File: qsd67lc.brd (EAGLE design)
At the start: 160 x 100 mm, 65 parts, among them CON1 RIA-AKL-230-04, CON2 RIA-AKL-230-04, CON3 RIA-AKL-230-03, IC1 MEGA8-P, IC2 BTS555E3146, IC3 MAX3232CPE, IC4 LM2576S, IC5 FT232RL, IC6 ISO7221A, T1 BCR141, U1 HC_05, X2 RS232

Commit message: first placement of all parts
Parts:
- LED4: value (none) -> green
- LED5: value (none) -> orange
- moved C17 401.5 mm to (67.3, 26.7)
- moved C18 401.5 mm to (67.3, 20.3), flipped to the bottom, turned to 180 degrees
- moved IC6 387.4 mm to (67.3, 20.3), turned to 180 degrees
- moved C15 366.9 mm to (57.1, 29.2)
- moved C16 359.5 mm to (66.0, 8.89)
- moved R19 353.1 mm to (68.6, 12.7)
- moved R18 344.8 mm to (61.0, 12.7)
- moved LED5 341.1 mm to (69.8, 8.89), turned to 270 degrees
- moved C14 333.0 mm to (57.1, 17.8), turned to 180 degrees
- moved LED4 332.8 mm to (62.2, 8.89), turned to 270 degrees
- moved C13 331.9 mm to (57.1, 21.6)
- moved R10 281.7 mm to (29.2, 41.9), flipped to the bottom, turned to 90 degrees
- moved IC5 281.5 mm to (57.1, 20.3), turned to 90 degrees
- moved S1 134.6 mm to (64.8, 47.0), turned to 180 degrees
- moved R4 129.5 mm to (57.1, 2.54)
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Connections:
- net N$25 renamed USB_TX_LED
- net RS232_RX: no longer IC6.2
- net RS232_TX: no longer IC6.3
- net RXD_RS232: now also IC6.2
- net TXD_RS232: now also IC6.3
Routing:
- net 12V_OUT: track 18.3 -> 14.3 mm
- added copper zone on layer 1, net GND
- added copper zone on layer 16, net GND

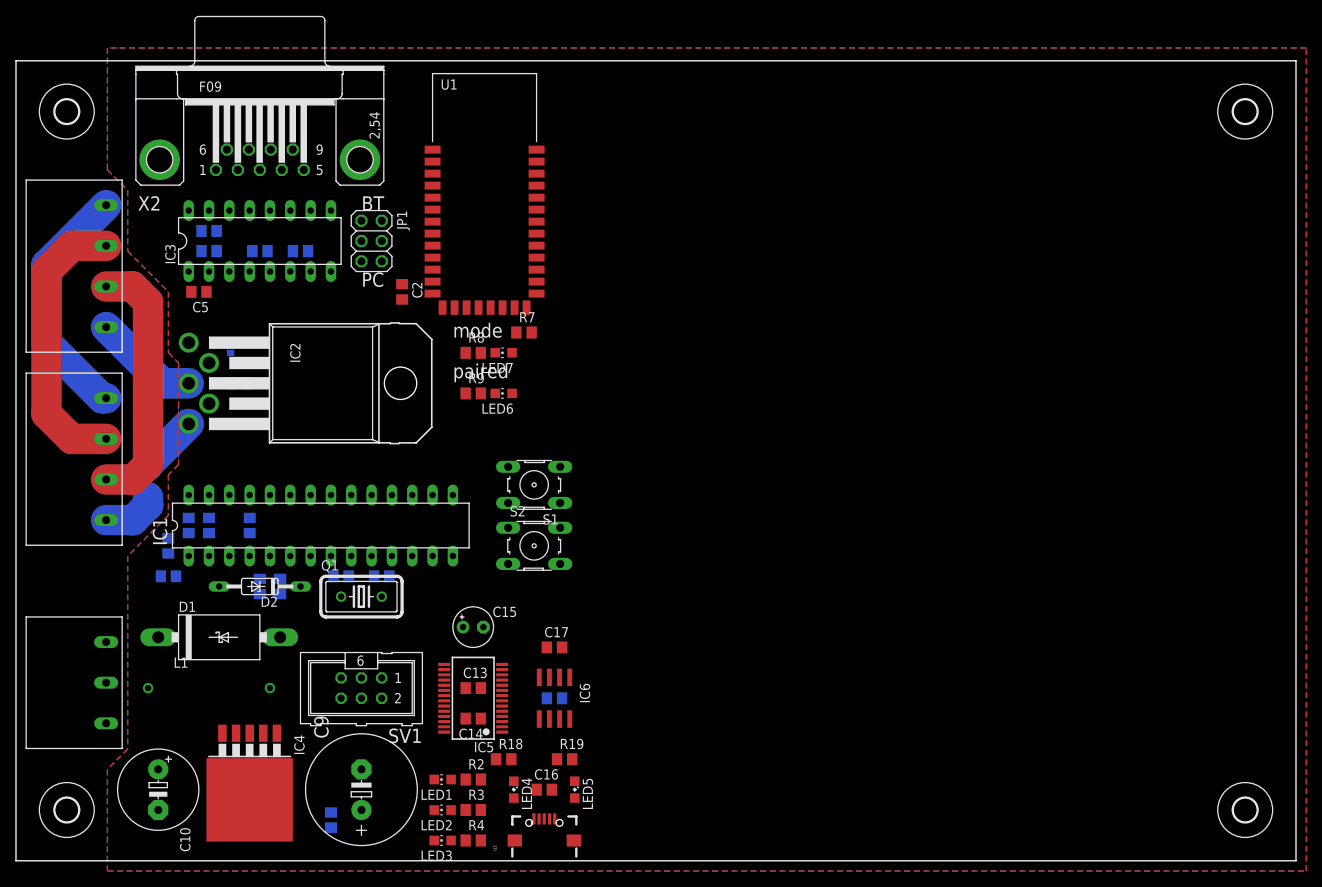
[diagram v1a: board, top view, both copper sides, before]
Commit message: working commit: * moved drill hole * removed 1 button * replaced status leds * moved ground planes
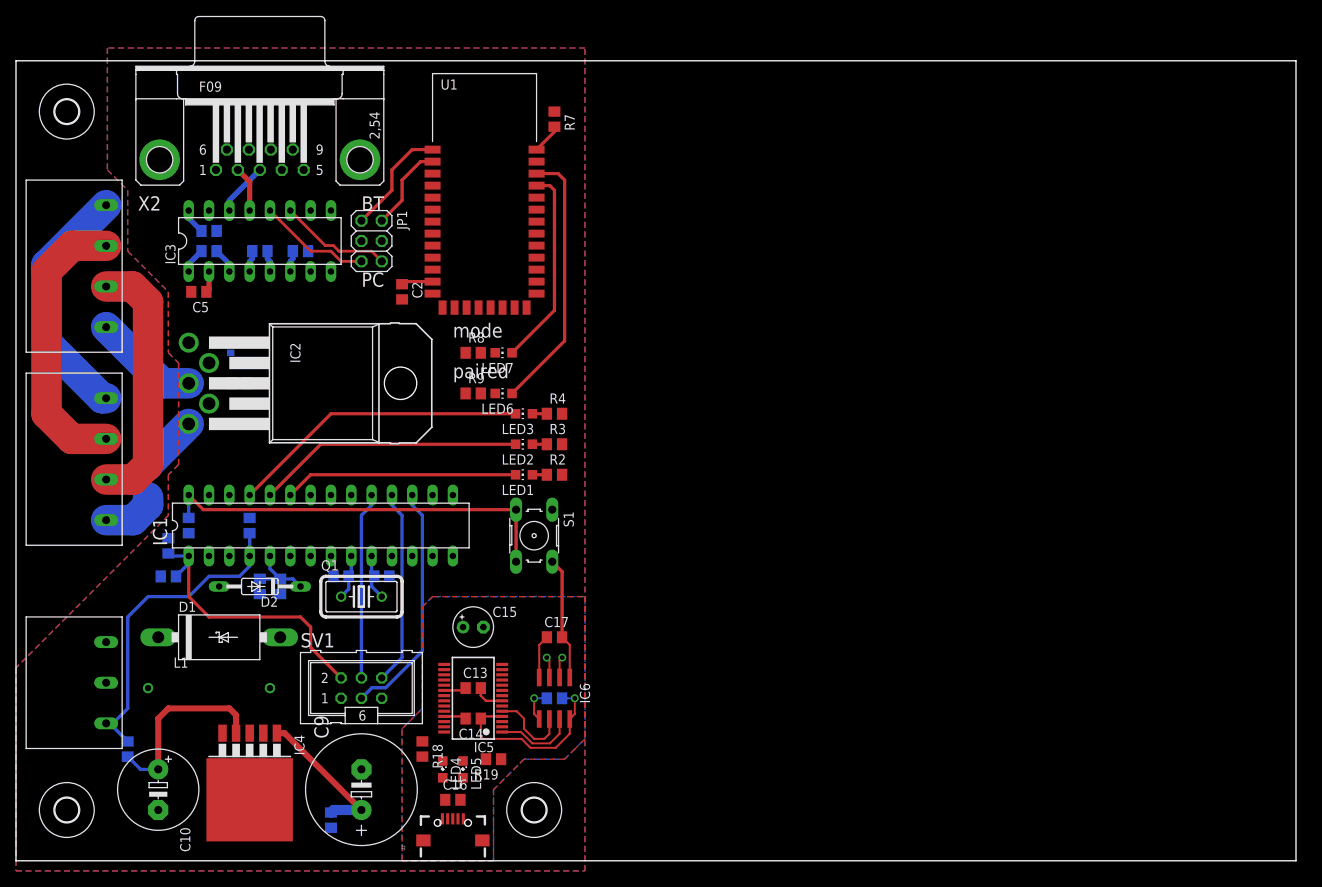
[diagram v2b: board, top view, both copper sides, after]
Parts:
- removed H2: MOUNT-HOLE3.0, holes:3,0
- removed R5: 10k, rcl:R0805
- removed S2: (no value), switch-omron:B3F-10XX
- added R14: 10k, rcl:R0805
- moved H3 88.9 mm to (64.8, 6.35)
- moved LED3 54.3 mm to (63.5, 55.9)
- moved R4 54.3 mm to (67.3, 55.9)
- moved LED2 46.8 mm to (63.5, 52.1)
- moved R3 46.8 mm to (67.3, 52.1)
- moved LED1 39.4 mm to (63.5, 48.3)
- moved R2 39.4 mm to (67.3, 48.3)
- moved R7 26.9 mm to (67.3, 92.7), turned to 270 degrees
- moved LED5 14.2 mm to (55.9, 11.4)
- moved C16 11.5 mm to (54.6, 7.62)
- moved U2 11.4 mm to (54.6, 2.54)
- moved R18 10.2 mm to (50.8, 14.0), turned to 270 degrees
- moved LED4 9.25 mm to (53.3, 11.4)
- moved R19 8.89 mm to (59.7, 12.7), turned to 180 degrees
- moved S1 6.35 mm to (64.8, 40.6), turned to 270 degrees
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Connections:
- removed net IGN0_IN: R13.2
- removed net N$8: IC1.27, R5.2, S2.3, S2.4
- net +3V3: now also R14.2; no longer S2.1, S2.2
- net GND: no longer R5.1
- net IGN0: now also R13.2
- net QS+: now also R14.1
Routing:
- net N$12: track 0.00 -> 51.0 mm
- net +3V3: track 0.00 -> 46.2 mm
- net QS+: track 0.00 -> 40.5 mm
- net N$9: track 0.00 -> 37.4 mm
- net RESET: track 0.00 -> 35.7 mm
- net N$1: track 0.00 -> 33.3 mm
- net PAIRED_STATE: track 0.00 -> 33.2 mm
- net MOSI: track 0.00 -> 30.1 mm
- net N$7: track 0.00 -> 29.2 mm
- net WORK_MODE: track 0.00 -> 25.0 mm
- net MISO: track 0.00 -> 24.4 mm
- net VCCIO_USB: track 0.00 -> 23.7 mm, vias 0 -> 1
- net SCK: track 0.00 -> 23.4 mm
- net +12V: track 13.2 -> 31.7 mm
- net RXD_RS232: track 0.00 -> 16.7 mm, vias 0 -> 1
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- added copper zone on layer 1, net GND_USB
- added copper zone on layer 16, net GND_USB

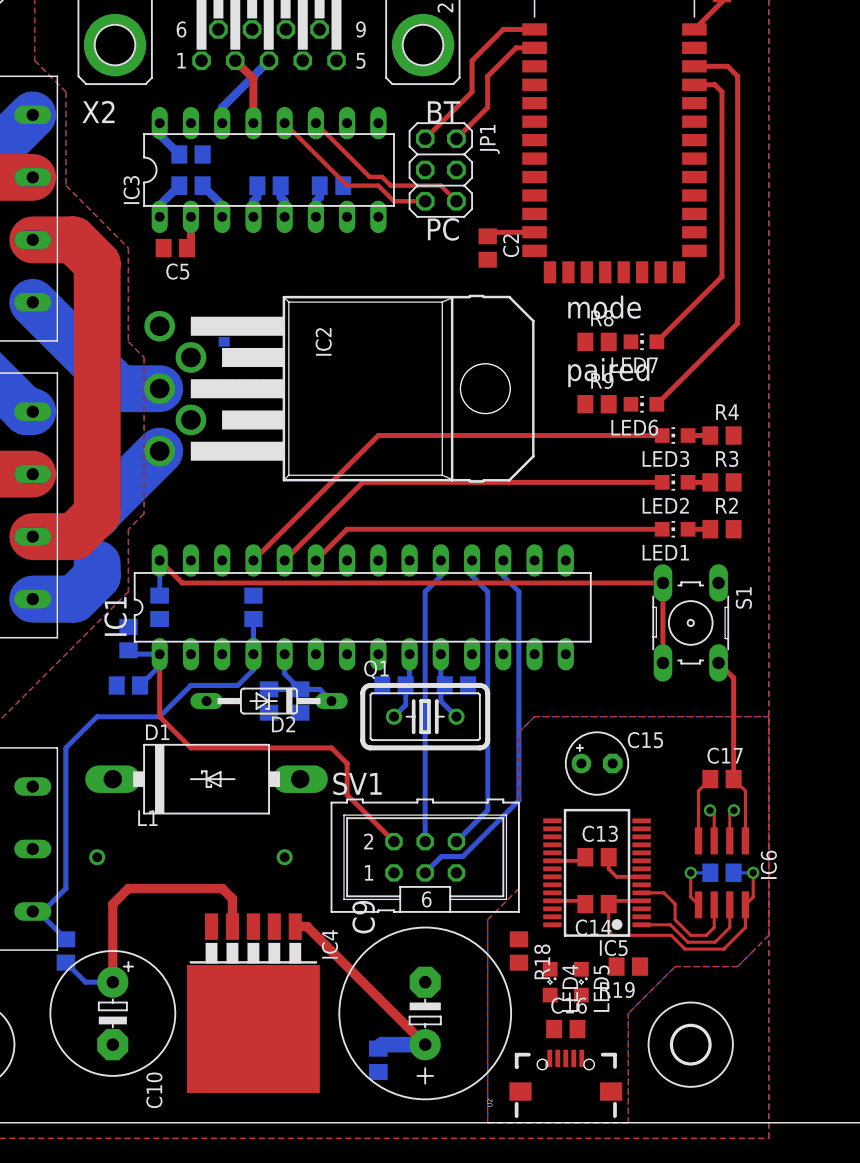
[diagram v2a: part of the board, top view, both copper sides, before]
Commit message: routed ftdi part
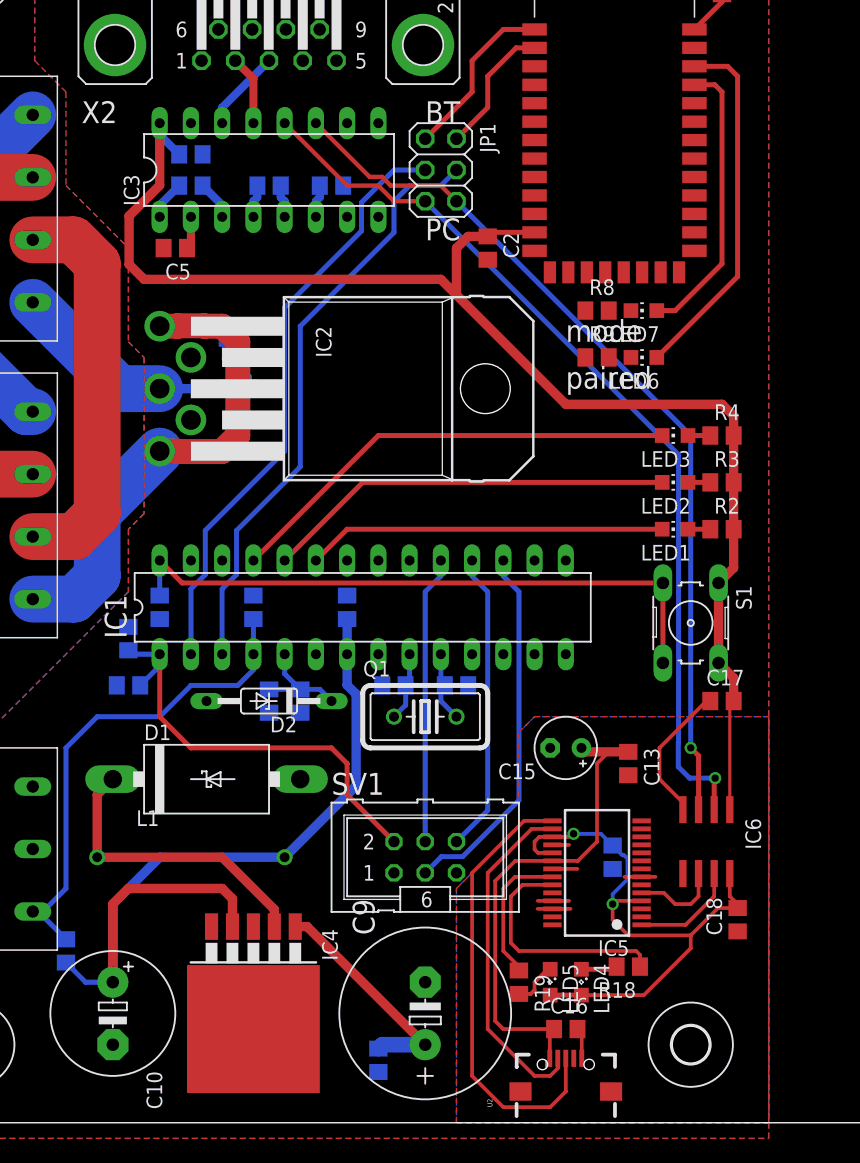
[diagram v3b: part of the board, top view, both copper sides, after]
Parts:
- added C19: 100n, rcl:C0805
- moved R18 8.98 mm to (59.7, 12.7), turned to 180 degrees
- moved R19 8.98 mm to (50.8, 11.4), turned to 270 degrees
- moved C13 8.03 mm to (59.7, 29.2), turned to 270 degrees
- moved C17 6.35 mm to (67.3, 34.3)
- moved C14 4.02 mm to (58.4, 21.6), flipped to the bottom, turned to 270 degrees
- moved C18 4.02 mm to (68.6, 16.5), flipped to the top, turned to 90 degrees
- moved LED6 3.81 mm to (61.0, 62.2)
- moved R9 3.81 mm to (57.1, 62.2)
- moved C15 2.84 mm to (54.6, 30.5), turned to 180 degrees
- moved IC6 2.84 mm to (66.0, 22.9)
- moved LED7 2.54 mm to (61.0, 66.0)
- moved R8 2.54 mm to (57.1, 66.0)
- moved LED4 2.54 mm to (55.9, 11.4)
- moved LED5 2.54 mm to (53.3, 11.4)
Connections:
- net +3V3: now also C19.1
- net GND: now also C19.2
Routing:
- net +3V3: track 46.2 -> 181.5 mm
- net RXD_RS232: track 16.7 -> 74.7 mm
- net TXD_RS232: track 16.7 -> 71.7 mm
- net TXD: track 0.00 -> 48.7 mm
- net RXD: track 0.00 -> 48.7 mm
- net VCC_USB: track 2.80 -> 41.8 mm
- net USB_D+: track 0.00 -> 36.7 mm
- net USB_D-: track 0.00 -> 27.8 mm
- net 12V_OUT: track 14.3 -> 39.7 mm
- net N$22: track 0.00 -> 24.4 mm
- net VCCIO_USB: track 23.7 -> 48.0 mm, vias 1 -> 2
- net USB_RX_LED: track 0.00 -> 19.4 mm
- net USB_TX_LED: track 0.00 -> 11.6 mm
- net GND: track 5.42 -> 11.5 mm
- net +12V: track 31.7 -> 37.1 mm
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
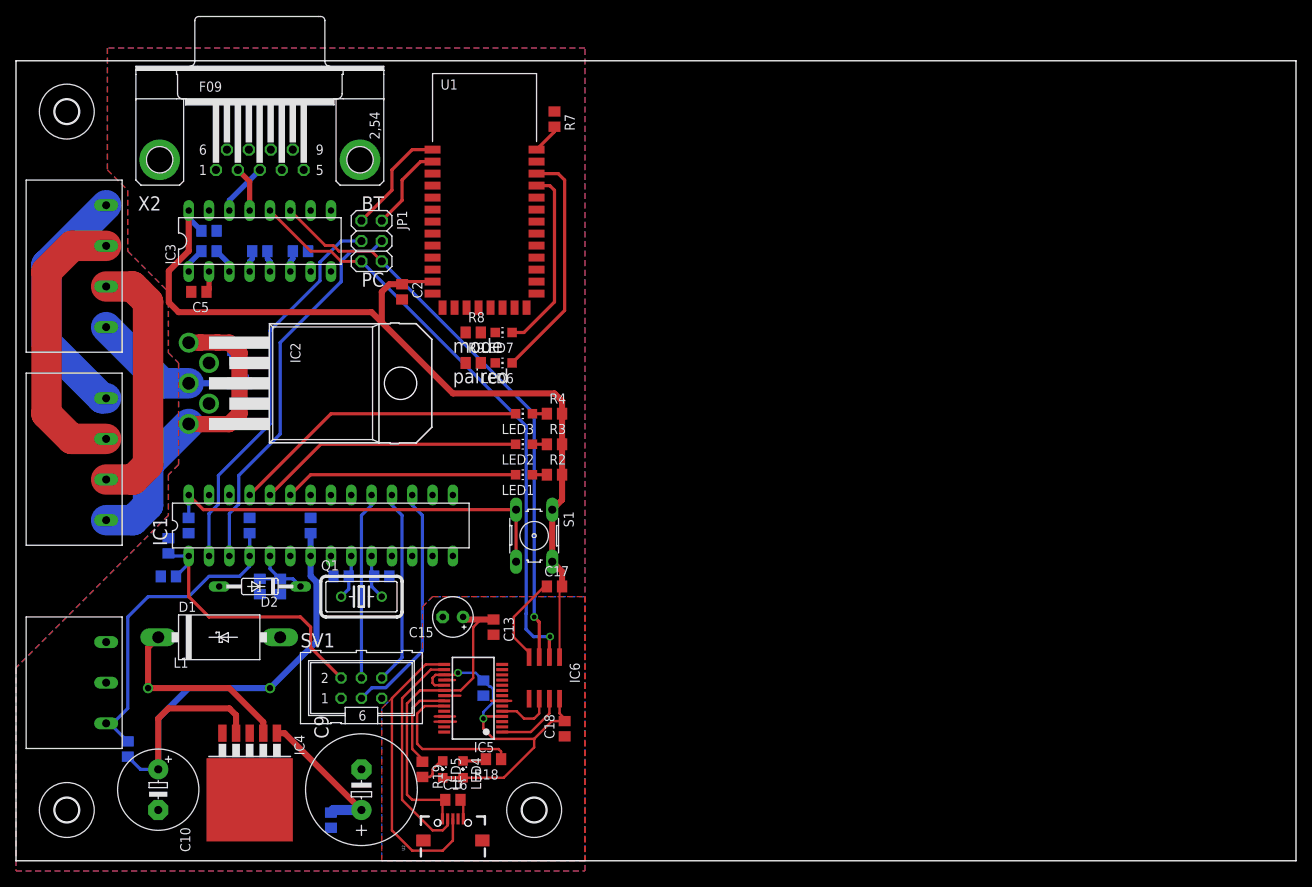
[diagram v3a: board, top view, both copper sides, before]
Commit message: finished layout added some test probe pins to 3v3 12V and GND added lables to leds, connectors and pinheads
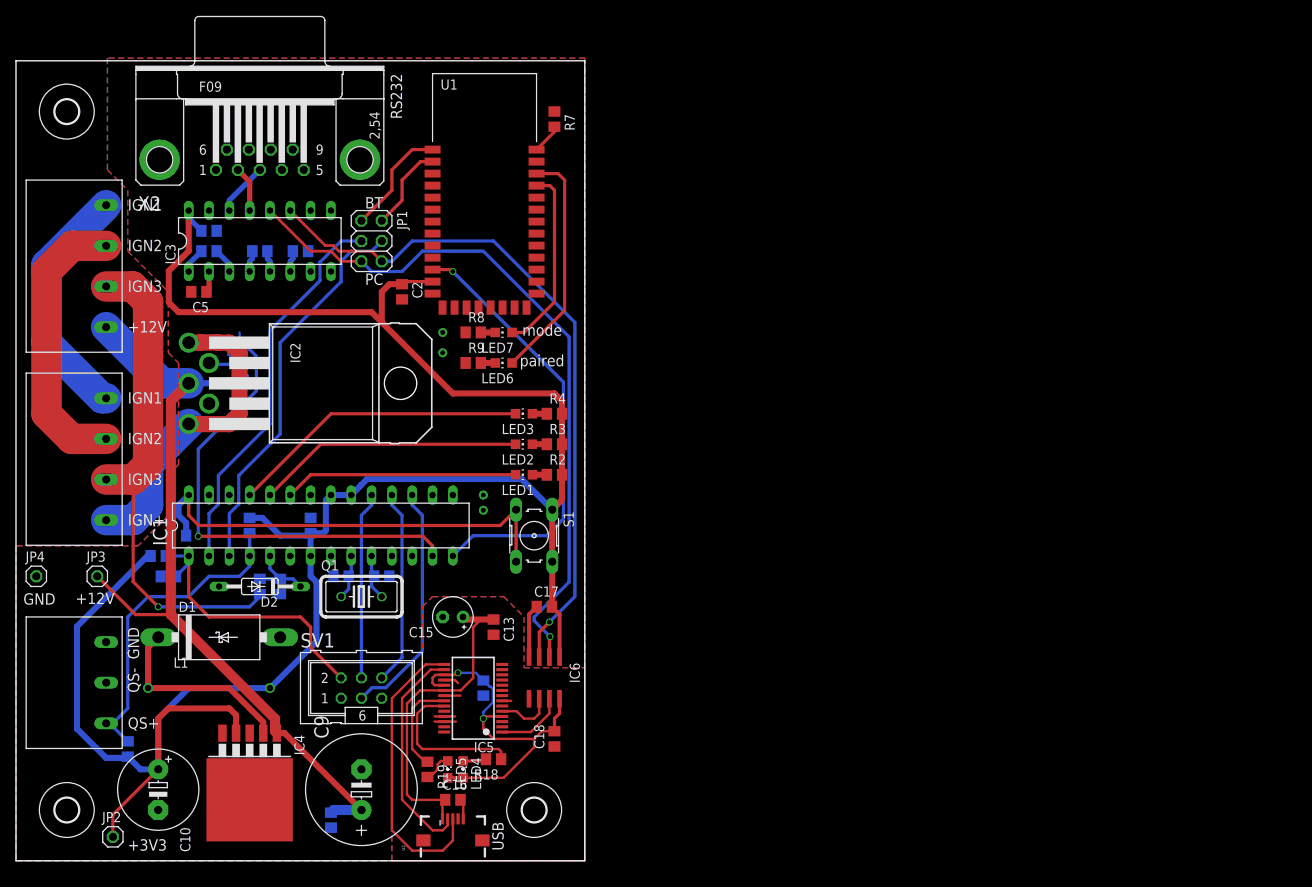
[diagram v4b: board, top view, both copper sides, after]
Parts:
- added JP2, JP3, JP4: (no value), pinhead:1X01
- moved C17 2.84 mm to (66.0, 31.8)
- moved C18 1.80 mm to (67.3, 15.2)
- moved R1 1.80 mm to (17.8, 38.1), turned to 0 degrees
- moved R6 1.80 mm to (20.3, 40.6), turned to 180 degrees
- moved R19 0.64 mm to (51.4, 11.4)
- moved LED5 0.63 mm to (54.0, 11.4)
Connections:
- net +12V: now also JP3.1
- net +3V3: now also JP2.1
- net GND: now also JP4.1
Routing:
- net +3V3: track 181.5 -> 271.2 mm
- net +12V: track 37.1 -> 98.4 mm
- net IGN_CTL: track 0.00 -> 58.4 mm, vias 0 -> 1
- net HC05_RST: track 0.00 -> 55.0 mm, vias 0 -> 1
- net IGN0: track 32.4 -> 63.1 mm, vias 0 -> 1
- net TXD_RS232: track 71.7 -> 87.1 mm
- net RXD_RS232: track 74.7 -> 88.7 mm
- net N$12: track 51.0 -> 57.3 mm
- net N$16: track 5.03 -> 7.81 mm
- net N$14: track 0.00 -> 1.81 mm
- net N$13: track 0.00 -> 1.81 mm
- net VCCIO_USB: track 48.0 -> 46.4 mm
- net GND_USB: track 13.6 -> 12.8 mm
- net GND: track 11.5 -> 11.6 mm, vias 0 -> 4
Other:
- board size 160 x 100 mm -> 71.1 x 100 mm
- board text added: "+12V"
- board text added: "+3V3"
- board text added: "GND"
- board text added: "IGN+"
- board text added: "IGN1"
- board text added: "IGN2"
- board text added: "IGN3"
- board text added: "QS+"
- board text added: "QS-"
- board text added: "RS232"
- board text added: "USB"

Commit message: started development of v2 prototype containing OBDII diagnostics capabilities.
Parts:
- C1, C11, C19, C2, C5, C6, C7, C8: value 100n -> 100nF
- C15: value (none) -> 4,7µF
- C3, C4: value 15p -> 15pF
- Q1: value (none) -> 16MHz
- R2, R3, R4, R8, R9: value 220 -> 220R
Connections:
- removed net QS-: CON3.P$2
- net GND: now also CON3.P$2
